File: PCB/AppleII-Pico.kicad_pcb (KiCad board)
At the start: 2 copper layers, 107.2 x 56.7 mm, 29 parts, among them J1 Apple II, J2 DB15_Female_HighDensity_Mount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, J3 NOPAL, J4 Conn_02x08_Odd_Even, U1 74LCX16245, U2 74LCX16245, U5 PALCE16V8H, U6 Pi PICO, U7 AZ1117

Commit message: DRC fixes
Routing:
- net GND: track 161.4 -> 171.8 mm, vias 16 -> 19
- net A7: track 10.7 -> 12.5 mm
- net B2: track 84.3 -> 85.3 mm
- net Net-(R11-Pad1): track 62.8 -> 63.6 mm
- net G2: track 95.3 -> 96.0 mm
- net LPHI0: track 36.9 -> 36.3 mm
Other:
- board text added: "∀2"
- board text removed: "V2"

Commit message: beauty tweaks
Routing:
- net LD0: track 50.6 -> 58.6 mm
- net LD1: track 48.0 -> 55.3 mm
- net LD7: track 43.8 -> 44.8 mm
- net nLSEL: track 17.6 -> 18.6 mm
- net LR\W: track 20.7 -> 21.6 mm
- net LD6: track 42.9 -> 43.7 mm

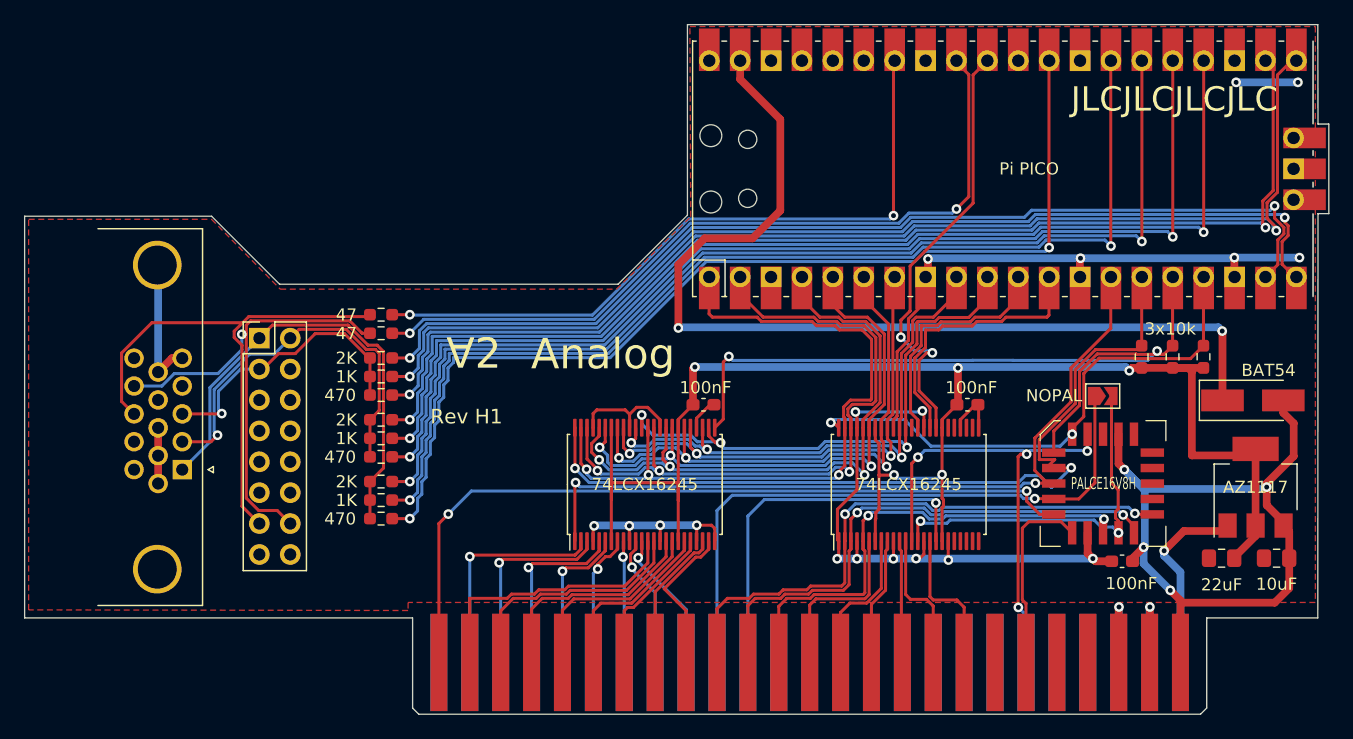
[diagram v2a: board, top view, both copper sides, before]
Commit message: incorporate feedback
 - Pico W antenna cutout
 - Pico RUN button
 - Break-away HD15A connector
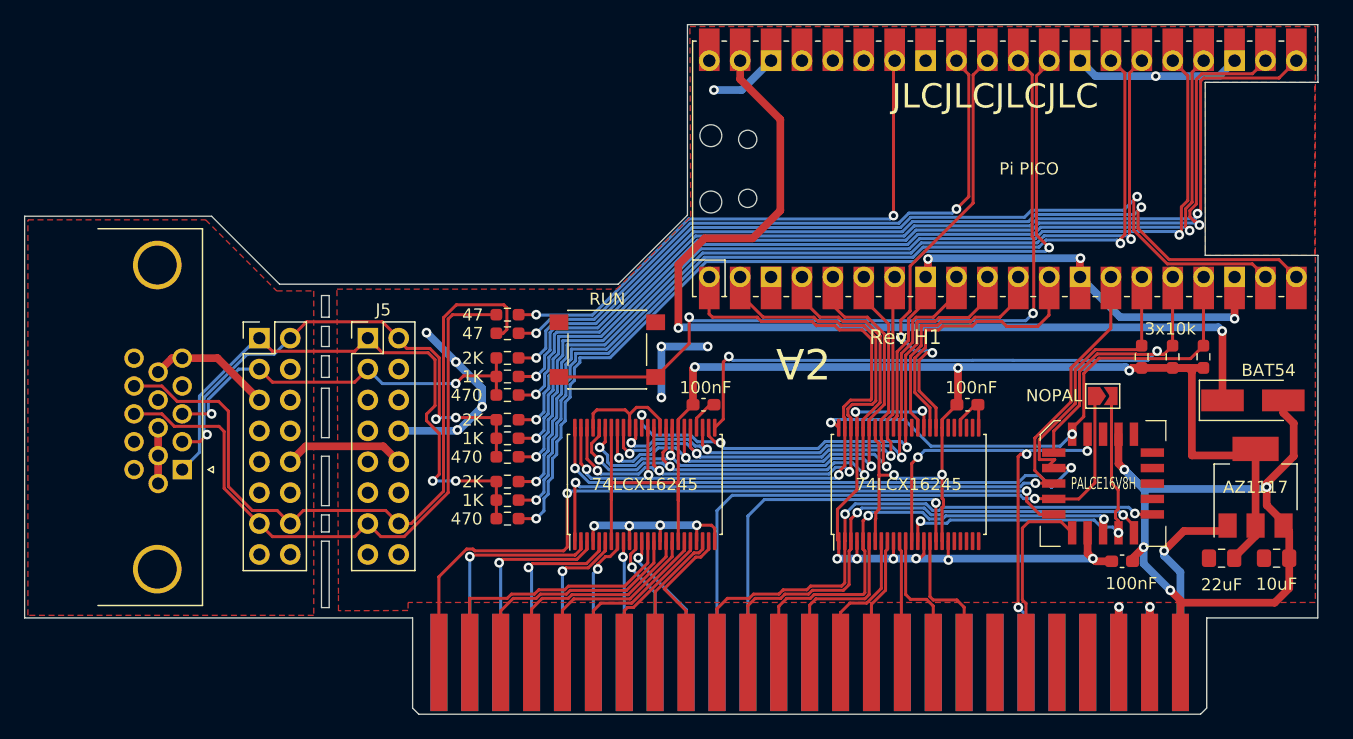
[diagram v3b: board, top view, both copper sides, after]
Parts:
- added J5: Conn_02x08_Odd_Even, Connector_PinHeader_2.54mm:PinHeader_2x08_P2.54mm_Vertical, F.Cu at (105.8, 103.6)
- added SW1: RUN, Button_Switch_SMD:SW_Push_1P1T_NO_6x6mm_H9.5mm, F.Cu at (125.5, 104.5)
- moved R1 10.4 mm to (117.3, 118.4)
- moved R10 10.4 mm to (117.3, 101.7)
- moved R11 10.4 mm to (117.3, 103.2)
- moved R2 10.4 mm to (117.3, 116.9)
- moved R3 10.4 mm to (117.3, 115.4)
- moved R4 10.4 mm to (117.3, 113.3)
- moved R5 10.4 mm to (117.3, 111.8)
- moved R6 10.4 mm to (117.3, 110.3)
- moved R7 10.4 mm to (117.3, 108.3)
- moved R8 10.4 mm to (117.3, 106.7)
- moved R9 10.4 mm to (117.3, 105.2)
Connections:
- U6 pad 30: unconnected-(U6-Pad30) -> RUN
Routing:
- net RUN: track 0.00 -> 64.0 mm, vias 0 -> 2
- net GND: track 171.8 -> 215.6 mm, vias 19 -> 25
- net VSYNC_OUT: track 41.2 -> 58.5 mm, vias 1 -> 0
- net B0: track 97.3 -> 83.7 mm
- net B2: track 85.3 -> 72.5 mm
- net G2: track 96.0 -> 84.6 mm
- net B1: track 86.2 -> 74.9 mm
- net R2: track 89.7 -> 78.7 mm
- net G1: track 91.6 -> 80.6 mm
- net Net-(R11-Pad1): track 63.6 -> 53.3 mm
- net Net-(R10-Pad1): track 57.4 -> 47.0 mm
- net R0: track 84.9 -> 74.5 mm
- net R1: track 89.2 -> 79.4 mm
- net GREEN_OUT: track 32.2 -> 42.0 mm, vias 1 -> 3
- net BLUE_OUT: track 23.5 -> 33.2 mm, vias 1 -> 2
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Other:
- board size 107.2 x 56.7 mm -> 106.3 x 56.7 mm
- board text removed: "Analog"

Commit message: RUN => Pico Reset
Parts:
- SW1: value RUN -> Pico Reset
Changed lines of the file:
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@@
       (effects (font (size 1 1) (thickness 0.15)))
     )
-    (fp_text value "RUN" (at 0 4.15) (layer "F.SilkS")
+    (fp_text value "Pico Reset" (at 0 4.15) (layer "F.SilkS")
       (effects (font (size 1 1) (thickness 0.15)))
     )

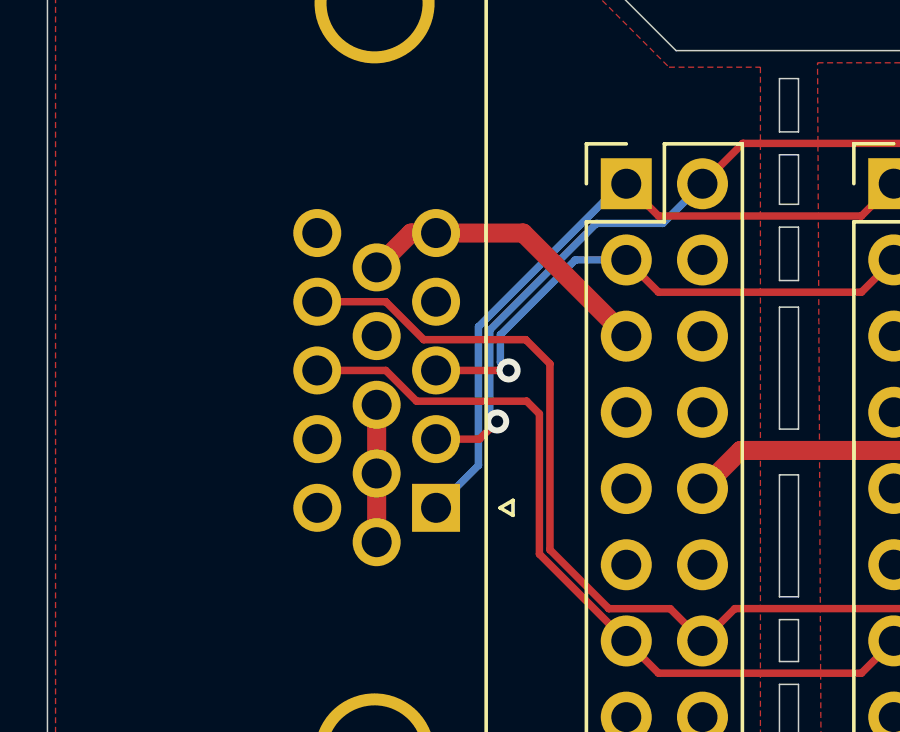
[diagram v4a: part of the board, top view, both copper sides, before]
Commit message: fix db15hd footprint
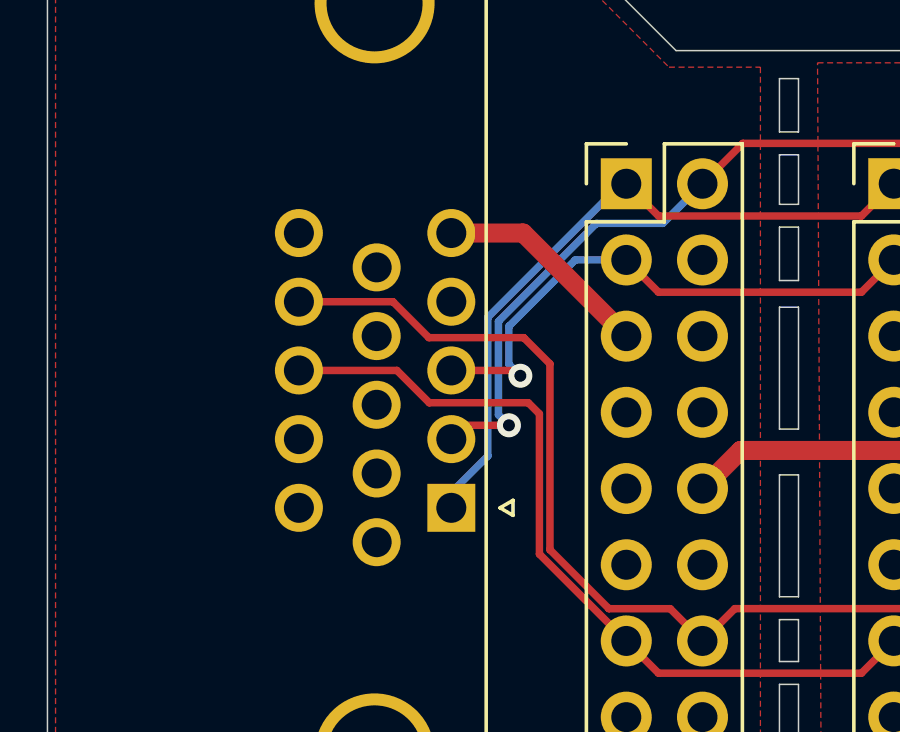
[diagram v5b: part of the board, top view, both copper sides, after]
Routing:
- net GND: track 215.6 -> 208.1 mm
- net HSYNC_OUT: track 53.5 -> 54.1 mm
- net VSYNC_OUT: track 58.5 -> 59.1 mm
